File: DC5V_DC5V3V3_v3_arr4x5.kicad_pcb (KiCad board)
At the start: 2 copper layers, 86 x 95.9 mm, 0 parts

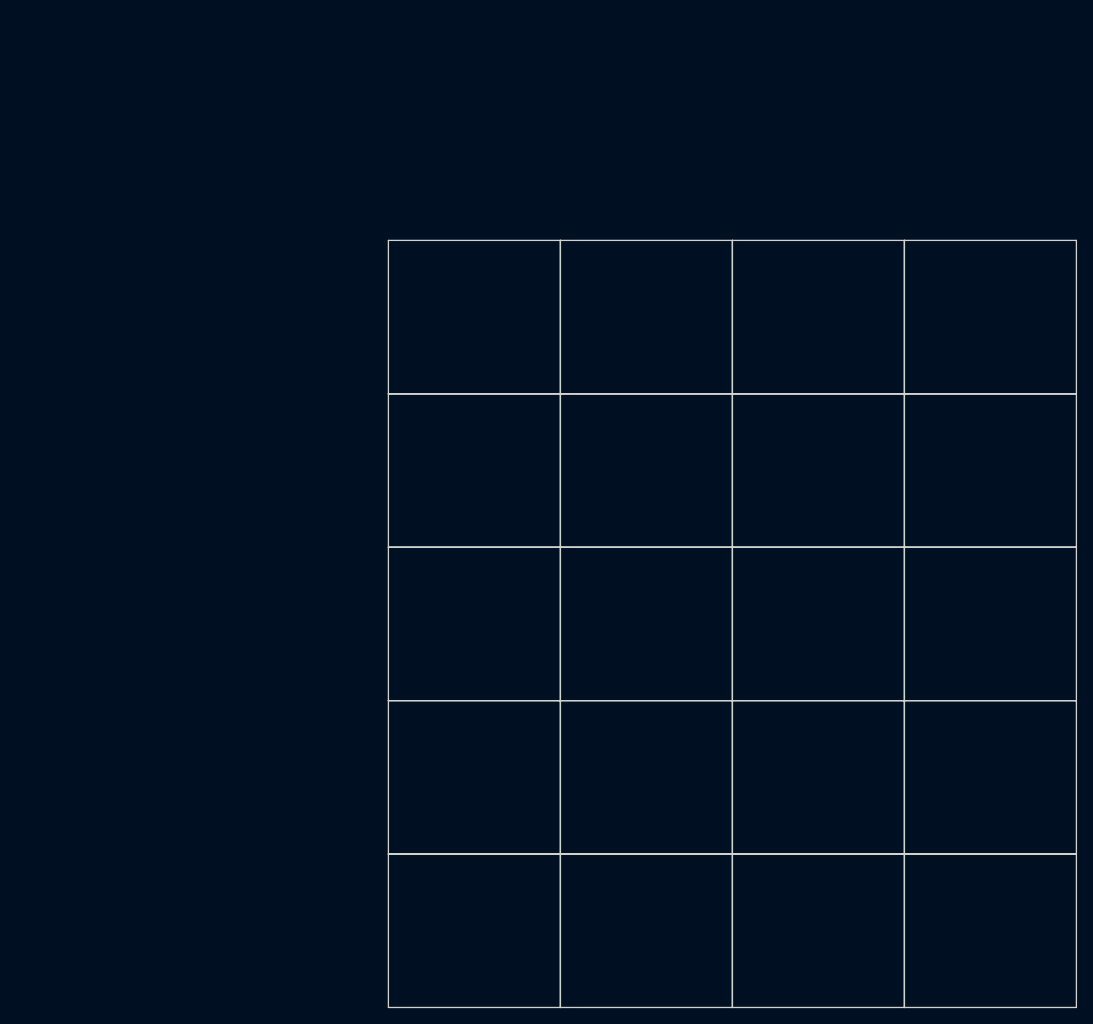
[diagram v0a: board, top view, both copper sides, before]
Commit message: Сформирован перечень элементов, 3D-модель, исправлены ошибки, реализована панелизация платы.
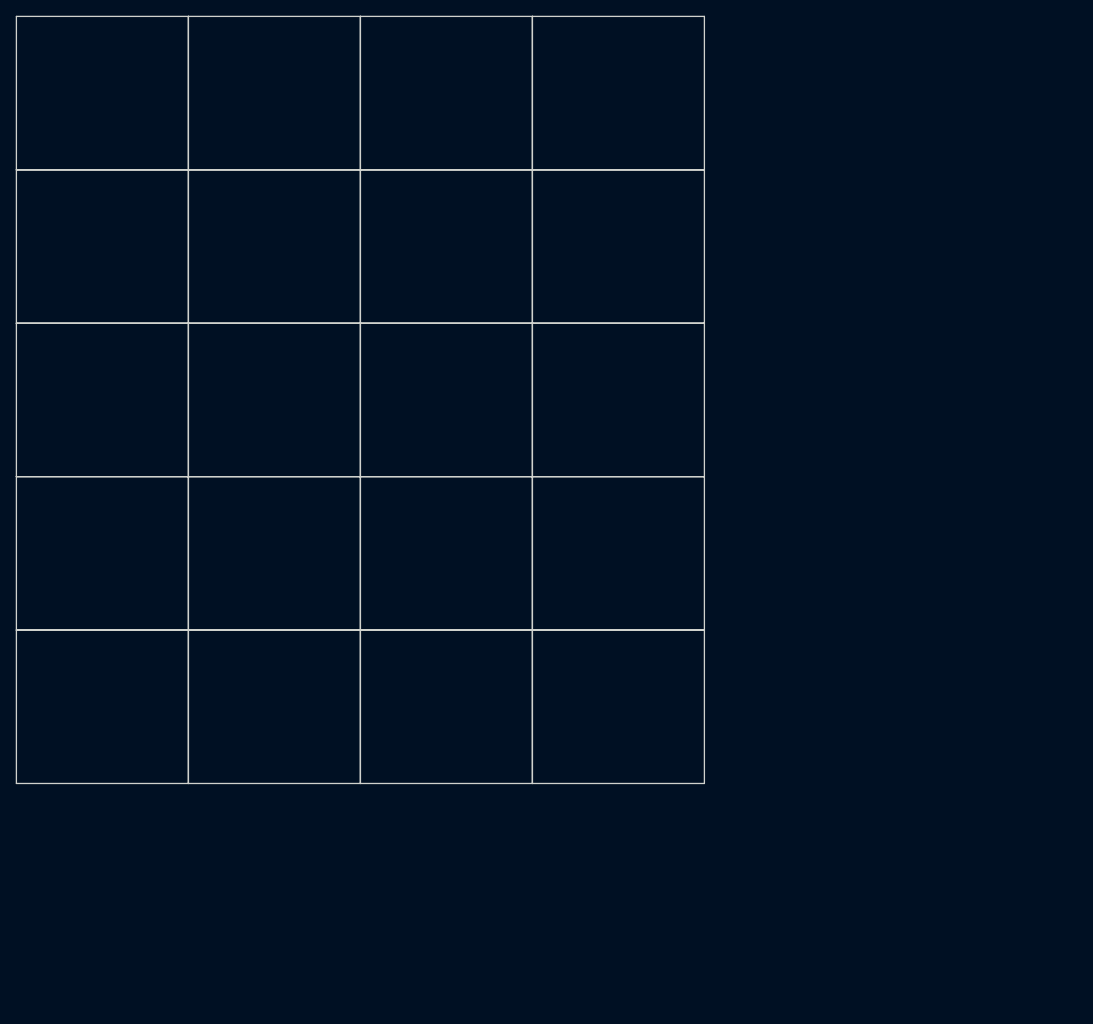
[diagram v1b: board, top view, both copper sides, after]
